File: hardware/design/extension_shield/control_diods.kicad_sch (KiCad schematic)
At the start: 20 parts, among them J10 Conn_01x02_Socket, J11 Conn_01x02_Socket, J12 Conn_01x02_Socket, J5 Conn_01x02_Socket, J6 Conn_01x02_Socket, Q1 BC546, Q2 BC546, Q3 BC546, Q4 BC546, Q5 BC546

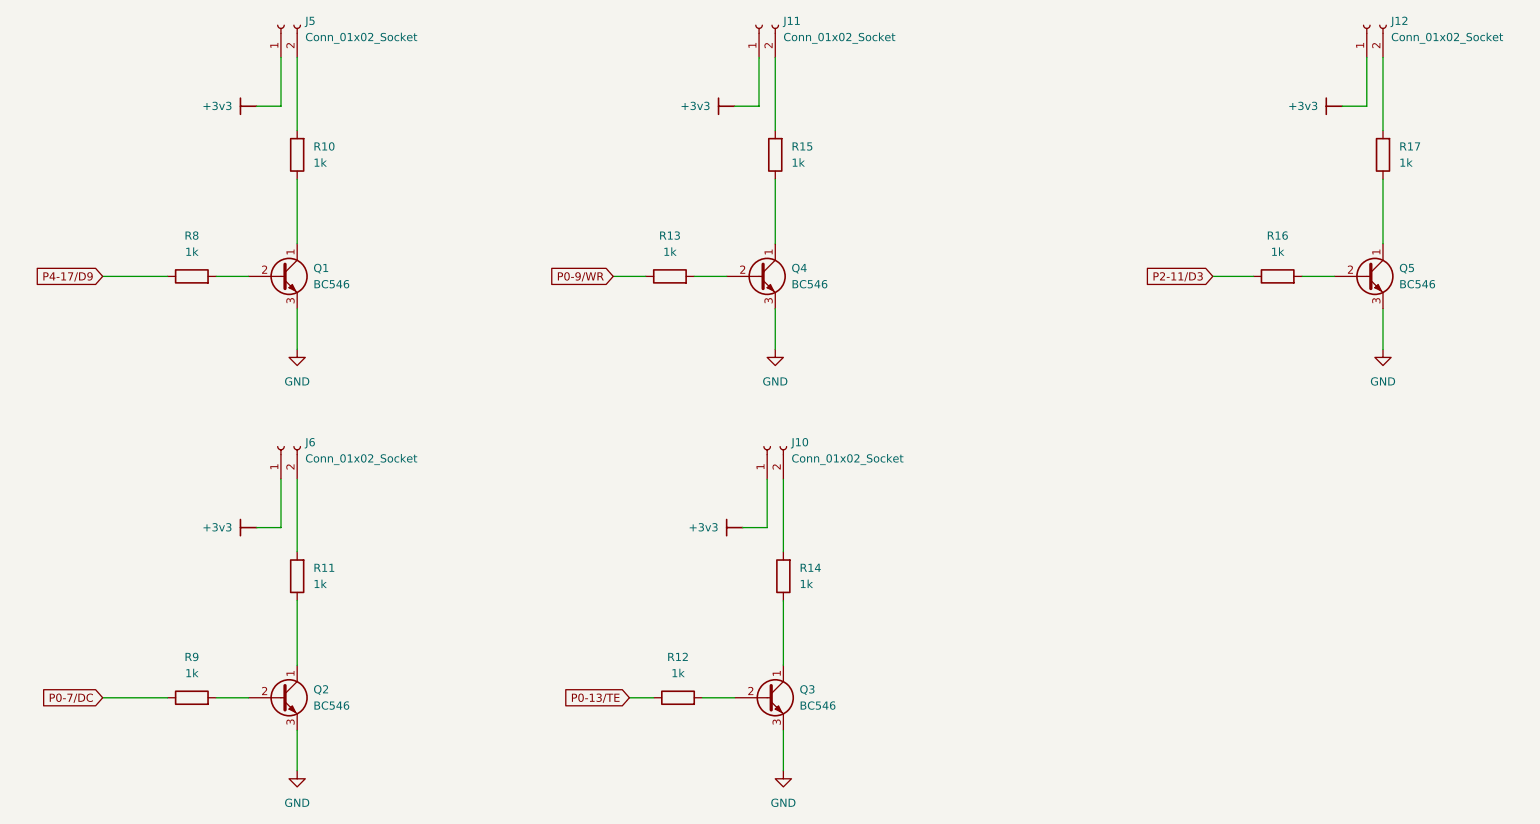
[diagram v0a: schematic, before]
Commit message: [HW/SHIELD] Adds Genereated PDF Schematic & Newer Version of Expansion Shield.
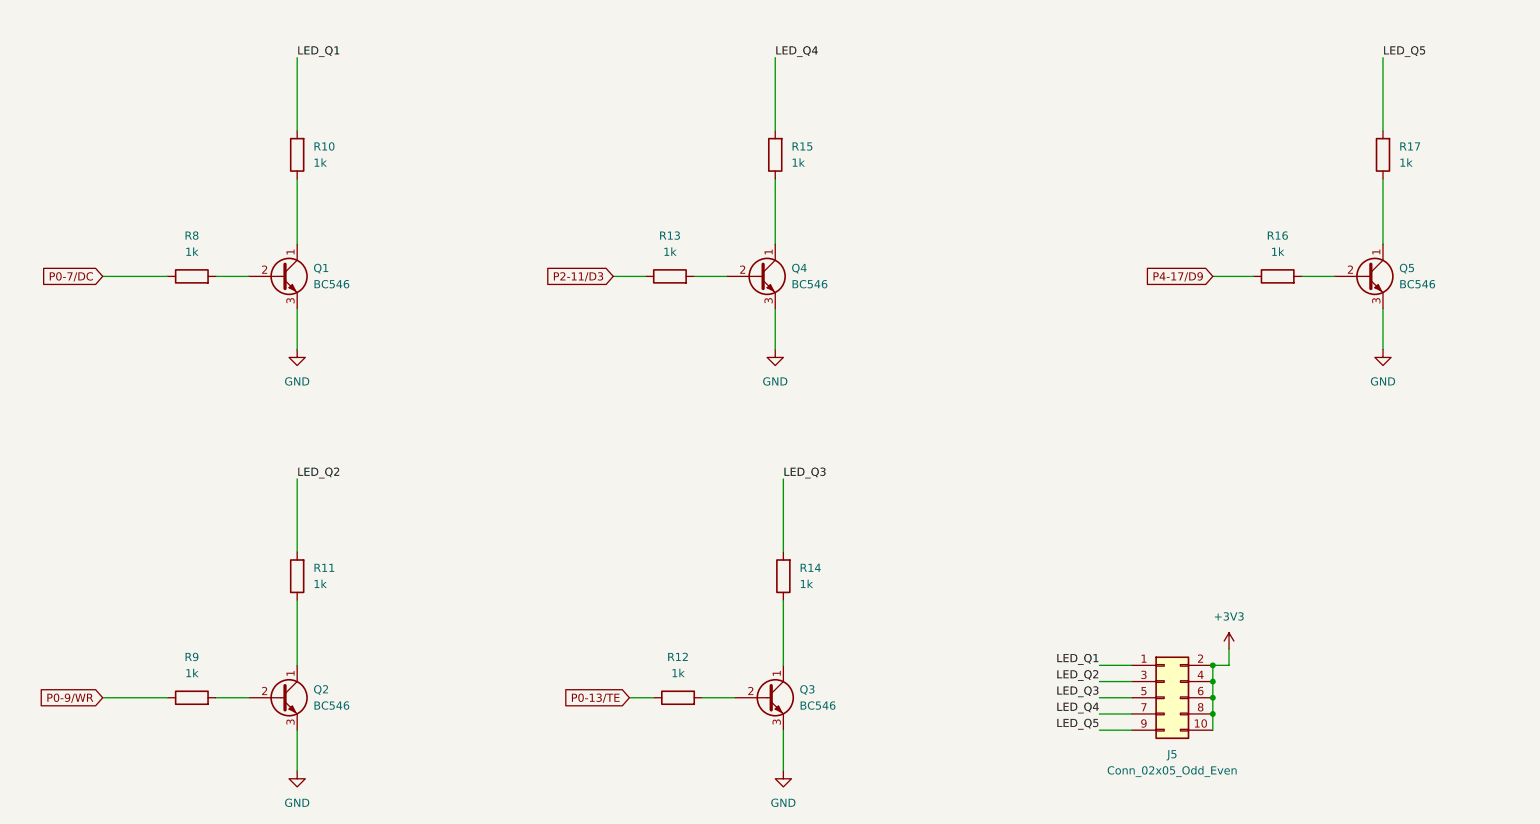
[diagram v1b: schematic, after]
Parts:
- removed J10, J11, J12, J5, J6: Conn_01x02_Socket, Connector_PinSocket_2.54mm:PinSocket_1x02_P2.54mm_Vertical, symbol Connector:Conn_01x02_Socket
- added J5: Conn_02x05_Odd_Even, Connector_PinSocket_2.54mm:PinSocket_2x05_P2.54mm_Vertical, symbol Connector_Generic:Conn_02x05_Odd_Even
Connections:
- net P0-7/DC: now also R8.1; no longer R9.1
- net P0-9/WR: now also R9.1; no longer R13.1
- net P2-11/D3: now also R13.1; no longer R16.1
- net P4-17/D9: now also R16.1; no longer R8.1
- net LED_Q1: now reaches R10.2
- net LED_Q1: now also J5.1 (Pin_1)
- net LED_Q3: now reaches R14.2
- net LED_Q3: now also J5.5 (Pin_5)
- net LED_Q5: now reaches R17.2
- net LED_Q5: now also J5.9 (Pin_9)
- net LED_Q4: now reaches R15.2
- net LED_Q4: now also J5.7 (Pin_7)
- net LED_Q2: now reaches R11.2
- net LED_Q2: now also J5.3 (Pin_3)
- new net +3V3: J5.10 (Pin_10), J5.2 (Pin_2), J5.4 (Pin_4), J5.6 (Pin_6), J5.8 (Pin_8)
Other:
- title: (none) -> Datalogger Expansion Shield
